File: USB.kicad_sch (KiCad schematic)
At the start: 8 parts, among them J23 USB_B_Micro, U19 CP2102N-A01-GQFN24

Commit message: Updated some symbols to use common libraries (and get rid of warnings.
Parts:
- D15: symbol Dash2-rescue:SP0503BAHT-Power_Protection -> Power_Protection:SP0503BAHT
- J23: symbol Dashboard-rescue:USB_B_Micro-Connector -> Connector:USB_B_Micro
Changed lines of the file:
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@@
 	)
 	(symbol
-		(lib_id "Dashboard-rescue:USB_B_Micro-Connector")
+		(lib_id "Connector:USB_B_Micro")
 		(at 76.2 109.22 0)
 		(unit 1)
@@
 			)
 		)
-		(property "Datasheet" "~"
+		(property "Datasheet" "https://www.molex.com/content/dam/molex/molex-dot-com/products/automated/en-us/salesdrawingpdf/105/105017/1050171001_sd.pdf"
 			(at 80.01 110.49 0)
 			(effects
@@
 	)
 	(symbol
-		(lib_id "Dash2-rescue:SP0503BAHT-Power_Protection")
+		(lib_id "Power_Protection:SP0503BAHT")
 		(at 100.33 121.92 0)
 		(unit 1)

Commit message: Updated comments.
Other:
- note added: "No changes made"
- note removed: "No change required"
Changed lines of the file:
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@@
 		)
 	)
-	(text "No change required\n"
+	(text "No changes made\n"
 		(exclude_from_sim no)
-		(at 15.24 21.59 0)
+		(at 177.8 180.34 0)
 		(effects
 			(font
 				(face "KiCad Font")
-				(size 5 5)
+				(size 1.524 1.524)
 				(thickness 1)
 				(bold yes)

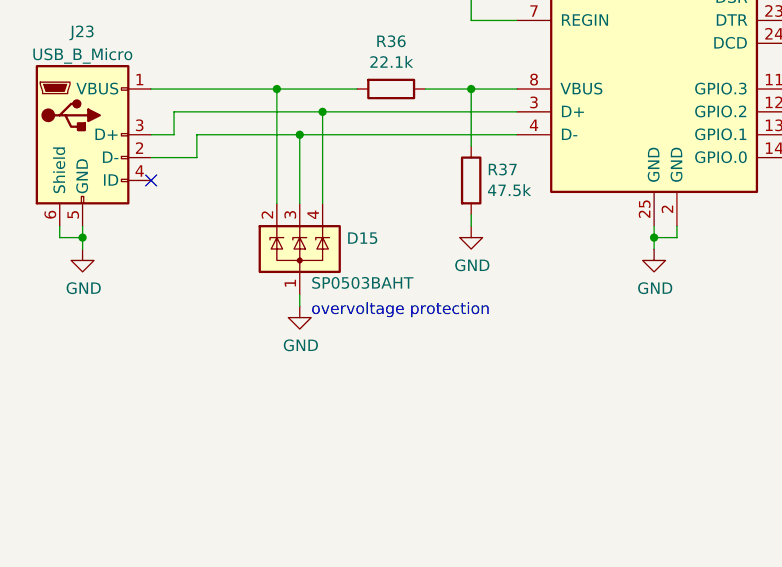
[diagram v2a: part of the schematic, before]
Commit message: Replaced unavailable parts
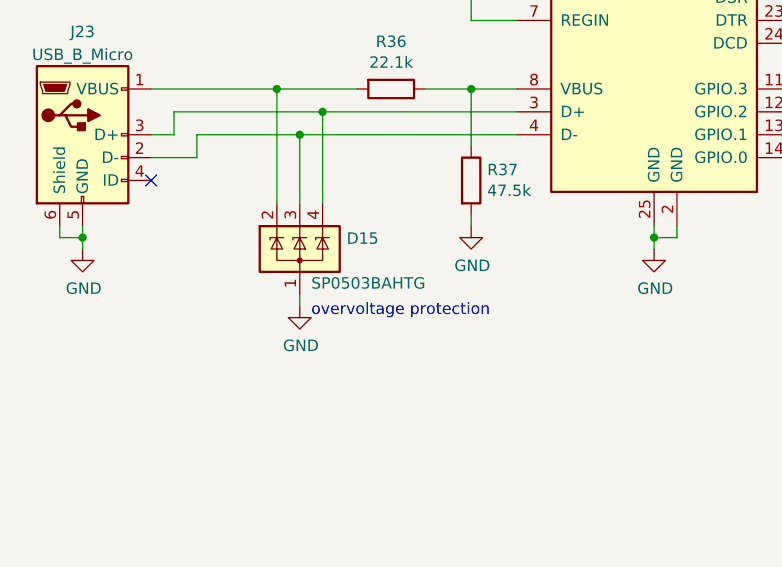
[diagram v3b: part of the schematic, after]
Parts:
- D15: value SP0503BAHT -> SP0503BAHTG
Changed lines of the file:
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@@
 			)
 		)
-		(property "Datasheet" "http://www.silabs.com/support%20documents/technicaldocs/cp2102n-datasheet.pdf"
+		(property "Datasheet" "https://www.mouser.com/ProductDetail/Silicon-Labs/CP2102N-A02-GQFN24?qs=u16ybLDytRYKabtL%2FE7DZA%3D%3D"
 			(at 140.97 123.19 0)
 			(effects
@@
 			)
 		)
-		(property "Value" "SP0503BAHT"
+		(property "Value" "SP0503BAHTG"
 			(at 101.6 125.73 0)
 			(effects
@@
 			)
 		)
-		(property "Datasheet" "http://www.littelfuse.com/~/media/files/littelfuse/technical%20resources/documents/data%20sheets/sp05xxba.pdf"
+		(property "Datasheet" "https://www.mouser.com/ProductDetail/Littelfuse/SP0503BAHTG?qs=uD%2FdkN7XIa0NTYXwHdELYA%3D%3D&srsltid=AfmBOopyYQ_2MkOf0VCWprrp-t78c1kQpFsdZaEYeSodgq0yTlD7vDtl"
 			(at 103.505 118.745 0)
 			(effects

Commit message: Filled in part numbers, exported BOM and made Excel file for working with it.
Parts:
- C41: P/N (none) -> GRM219R6YA475KA3D
- C42: P/N (none) -> C0805C104M5R
- D15: P/N (none) -> SP0503BAHTG
- R36: P/N (none) -> CRCW0805-22.1K-E3
- R37: P/N (none) -> CRCW0805-47.5K-E3
- R38: P/N (none) -> CRCW08051K00FKEAC
- U19: P/N (none) -> CP2102NA01GQFN24
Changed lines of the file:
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@@
+			)
+		)
+		(property "P/N" "CP2102NA01GQFN24"
+			(at 139.7 96.52 0)
+			(effects
+				(font
+					(size 1.27 1.27)
+				)
+				(hide yes)
 			)
 		)
@@
 			)
 		)
+		(property "P/N" "SP0503BAHTG "
+			(at 100.33 121.92 0)
+			(effects
+				(font
+					(size 1.27 1.27)
+				)
+				(hide yes)
+			)
+		)
 		(pin "1"
 		)
@@
 			)
 		)
+		(property "P/N" "CRCW0805-47.5K-E3"
+			(at 119.38 114.3 0)
+			(effects
+				(font
+					(size 1.27 1.27)
+				)
+				(hide yes)
+			)
+		)
 		(pin "1"
 		)
@@
 			)
 		)
+		(property "P/N" "CRCW0805-22.1K-E3"
+			(at 110.49 104.14 0)
+			(effects
+				(font
+					(size 1.27 1.27)
+				)
+				(hide yes)
+			)
+		)
 		(pin "1"
 		)
@@
 			)
 		)
+		(property "P/N" "CRCW08051K00FKEAC"
+			(at 121.92 76.2 0)
+			(effects
+				(font
+					(size 1.27 1.27)
+				)
+				(hide yes)
+			)
+		)
 		(pin "1"
 		)
@@
 			)
 		)
+		(property "P/N" "GRM219R6YA475KA3D"
+			(at 149.86 71.12 0)
+			(effects
+				(font
+					(size 1.27 1.27)
+				)
+				(hide yes)
+			)
+		)
 		(pin "1"
 		)
@@
 			(at 162.56 71.12 0)
 			(effects
+				(font
+					(size 1.27 1.27)
+				)
+				(hide yes)
+			)
+		)
+		(property "P/N" "C0805C104M5R"
+			(at 162.56 71.12 0)
+			(effects

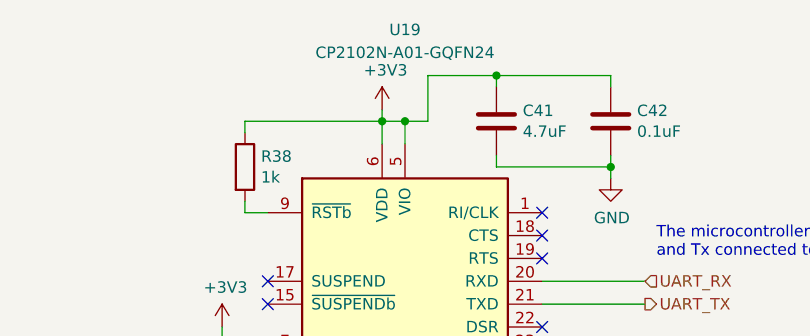
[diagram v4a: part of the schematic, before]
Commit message: Updated BOM a little (group parts better, usb pn was actually 1 number off).
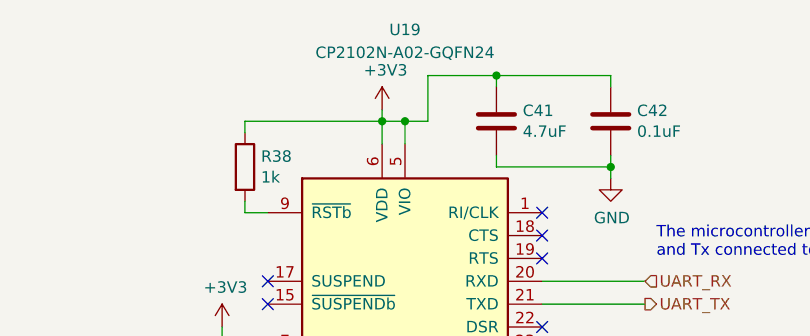
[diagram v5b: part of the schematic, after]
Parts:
- U19: value CP2102N-A01-GQFN24 -> CP2102N-A02-GQFN24; P/N CP2102NA01GQFN24 -> CP2102N-A02-GQFN24
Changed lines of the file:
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@@
 			)
 		)
-		(property "Value" "CP2102N-A01-GQFN24"
+		(property "Value" "CP2102N-A02-GQFN24"
 			(at 139.7 63.5 0)
 			(effects
@@
 			)
 		)
-		(property "Datasheet" "https://www.mouser.com/ProductDetail/Silicon-Labs/CP2102N-A02-GQFN24?qs=u16ybLDytRYKabtL%2FE7DZA%3D%3D"
+		(property "Datasheet" "https://www.mouser.com/ProductDetail/Silicon-Labs/CP2102N-A02-GQFN24?qs=u16ybLDytRYKabtL%2FE7DZA%3D%3D&srsltid=AfmBOorIqqALKMHmg5FULSneQVzUAM_9v_lkl9RlW5cuIFRYJJaXkOfo"
 			(at 140.97 123.19 0)
 			(effects
@@
 			)
 		)
-		(property "P/N" "CP2102NA01GQFN24"
+		(property "P/N" "CP2102N-A02-GQFN24"
 			(at 139.7 96.52 0)
 			(effects

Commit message: Added version update notes.
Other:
- note added: "- Updated USB chip"
- note removed: "No changes made"
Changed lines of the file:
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@@
+		)
+	)
+	(text "- Updated USB chip\n"
+		(exclude_from_sim no)
+		(at 178.054 169.926 0)
+		(effects
+			(font
+				(size 1.27 1.27)
+				(color 255 17 10 1)
+			)
+			(justify left bottom)
 		)
 	)
@@
 			)
 			(justify left bottom)
-		)
-	)
-	(text "No changes made\n"
-		(exclude_from_sim no)
-		(at 177.8 180.34 0)
-		(effects
-			(font
-				(face "KiCad Font")
-				(size 1.524 1.524)
-				(thickness 1)
-				(bold yes)
-				(color 255 2 13 1)
-			)
-			(justify left bottom)

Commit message: Moved version update notes.
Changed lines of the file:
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@@
 	(text "- Updated USB chip\n"
 		(exclude_from_sim no)
-		(at 178.054 169.926 0)
+		(at 178.054 180.086 0)
 		(effects
 			(font

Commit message: Added part numbers wheeeeeeeeeeeeeeeeeeeee
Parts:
- C41: JLCPCB# (none) -> C1779
- C42: JLCPCB# (none) -> C28233
- D15: JLCPCB# (none) -> C3040626
- R36: JLCPCB# (none) -> C17560
- R37: JLCPCB# (none) -> C17713
- R38: JLCPCB# (none) -> C17513
- U19: JLCPCB# (none) -> C969151
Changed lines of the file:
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@@
+			)
+		)
+		(property "JLCPCB#" " C969151"
+			(at 139.7 96.52 0)
+			(effects
+				(font
+					(size 1.27 1.27)
+				)
+				(hide yes)
 			)
 		)
@@
 			)
 		)
+		(property "JLCPCB#" ""
+			(at 76.2 109.22 0)
+			(effects
+				(font
+					(size 1.27 1.27)
+				)
+				(hide yes)
+			)
+		)
 		(pin "1"
 		)
@@
 			)
 		)
+		(property "JLCPCB#" "C3040626"
+			(at 100.33 121.92 0)
+			(effects
+				(font
+					(size 1.27 1.27)
+				)
+				(hide yes)
+			)
+		)
 		(pin "1"
 		)
@@
 			)
 		)
+		(property "JLCPCB#" "C17713"
+			(at 119.38 114.3 0)
+			(effects
+				(font
+					(size 1.27 1.27)
+				)
+				(hide yes)
+			)
+		)
 		(pin "1"
 		)
@@
 			)
 		)
+		(property "JLCPCB#" "C17560"
+			(at 110.49 104.14 0)
+			(effects
+				(font
+					(size 1.27 1.27)
+				)
+				(hide yes)
+			)
+		)
 		(pin "1"
 		)
@@
 			)
 		)
+		(property "JLCPCB#" "C17513"
+			(at 121.92 76.2 0)
+			(effects
+				(font
+					(size 1.27 1.27)
+				)
+				(hide yes)
+			)
+		)
 		(pin "1"
 		)
@@
 			)
 		)
+		(property "JLCPCB#" "C1779"
+			(at 149.86 71.12 0)
+			(effects
+				(font
+					(size 1.27 1.27)
+				)
+				(hide yes)
+			)
+		)
 		(pin "1"
 		)
@@
 			(at 162.56 71.12 0)
 			(effects
+				(font
+					(size 1.27 1.27)
+				)
+				(hide yes)
+			)
+		)
+		(property "JLCPCB#" "C28233"
+			(at 162.56 71.12 0)
+			(effects
